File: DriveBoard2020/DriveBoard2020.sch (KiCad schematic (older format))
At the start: 69 parts, among them SW0 SW_SPST, SW1 SW_Push, SW3 SW_Push, SW5 SW_Push, SW7 SW_Push, SW8 SW_Push, SW9 SW_Push, U1 MAX_3232, U2 MAX_3232, U3 OKI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

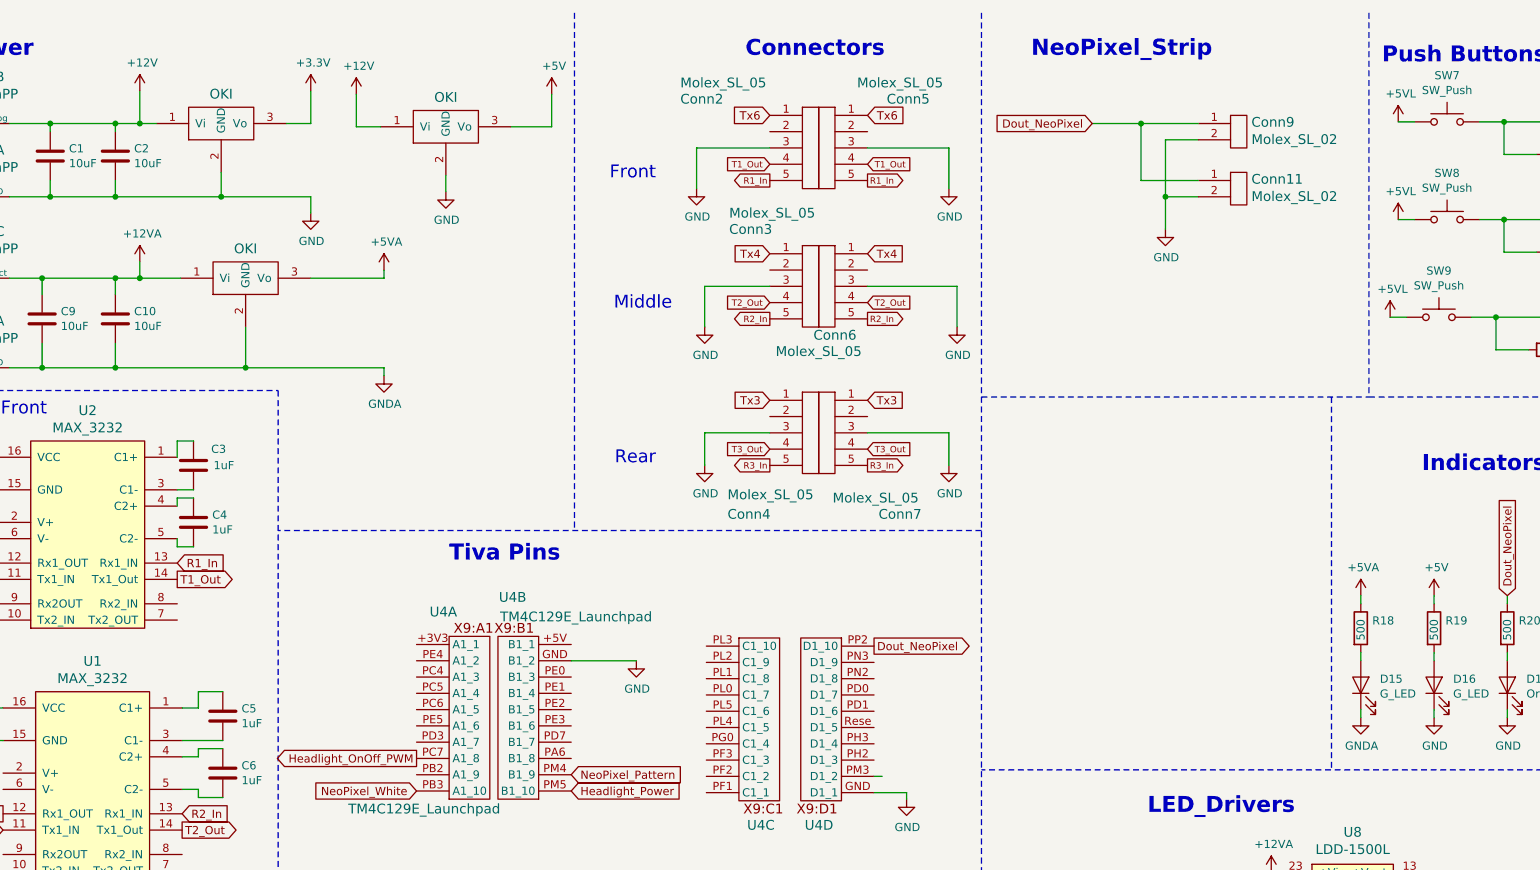
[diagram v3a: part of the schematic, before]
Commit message: cleaned up layout and generated gerbs
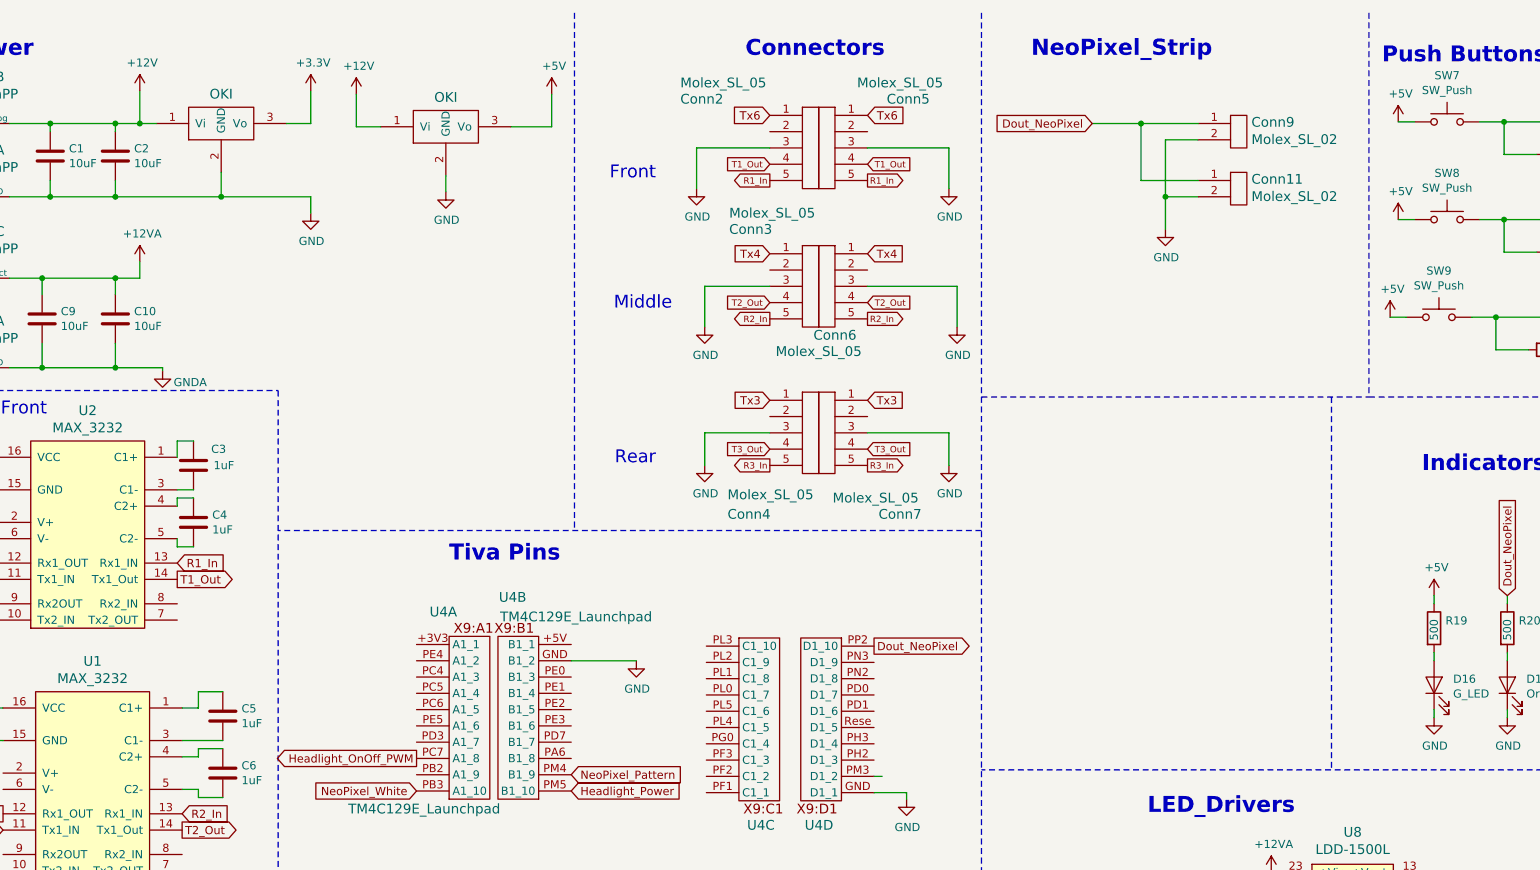
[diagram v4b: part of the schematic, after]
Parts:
- removed D15: G_LED, LED_SMD:LED_0603_1608Metric_Pad1.05x0.95mm_HandSolder, symbol Device:LED
- removed R18: 500, Resistor_SMD:R_0603_1608Metric_Pad1.05x0.95mm_HandSolder, symbol Device:R
- removed U7: OKI, MRDT_Devices:OKI_Horizontal, symbol DriveBoard2020-rescue:OKI-MRDT_Devices-DriveBoard2020-rescue
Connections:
- net +5VL is gone; now on net +5V: SW7.1, SW8.1, SW9.1
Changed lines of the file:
@@
 Indicators
-$Comp
-L Device:R R18
-U 1 1 5C07EDC4
-P 14120 4250
-F 0 "R18" H 14190 4296 50  0000 L CNN
-F 1 "500" V 14120 4175 50  0000 L CNN
-F 2 "Resistor_SMD:R_0603_1608Metric_Pad1.05x0.95mm_HandSolder" V 14050 4250 50  0001 C CNN
-F 3 "~" H 14120 4250 50  0001 C CNN
-	1    14120 4250
-	1    0    0    -1
-$EndComp
 $Comp
 L Device:R R20
@@
 	1    15545 4800
 	1    0    0    -1
-$EndComp
-$Comp
-L Device:LED D15
-U 1 1 5C07F18A
-P 14120 4600
-F 0 "D15" V 14158 4483 50  0000 R CNN
-F 1 "G_LED" V 14067 4483 50  0000 R CNN
-F 2 "LED_SMD:LED_0603_1608Metric_Pad1.05x0.95mm_HandSolder" H 14120 4600 50  0001 C CNN
-F 3 "~" H 14120 4600 50  0001 C CNN
-	1    14120 4600
-	0    -1   -1   0
 $EndComp
 $Comp
@@
 $EndComp
 Wire Wire Line
-	14120 4400 14120 4450
-Wire Wire Line
 	15020 4400 15020 4450
 Wire Wire Line
@@
 Wire Wire Line
 	15545 4750 15545 4800
-Wire Wire Line
-	14120 4100 14120 4050
 Text GLabel 15020 4050 1    50   Input ~ 0
 Dout_NeoPixel
@@
 Wire Wire Line
 	15020 4750 15020 4800
-Wire Wire Line
-	14120 4750 14120 4800
 $Comp
 L power:+12VA #PWR0149
@@
 Wire Wire Line
 	14620 6000 15070 6000
-$Comp
-L power:+5VA #PWR0152
-U 1 1 5C7B3BE6
-P 14120 4050
-F 0 "#PWR0152" H 14120 3900 50  0001 C CNN
-F 1 "+5VA" H 14135 4223 50  0000 C CNN
-F 2 "" H 14120 4050 50  0001 C CNN
-F 3 "" H 14120 4050 50  0001 C CNN
-	1    14120 4050
-	1    0    0    -1
-$EndComp
-$Comp
-L power:GNDA #PWR0156
-U 1 1 5C7A2B5E
-P 14120 4800
-F 0 "#PWR0156" H 14120 4550 50  0001 C CNN
-F 1 "GNDA" H 14125 4627 50  0000 C CNN
-F 2 "" H 14120 4800 50  0001 C CNN
-F 3 "" H 14120 4800 50  0001 C CNN
-	1    14120 4800
-	1    0    0    -1
-$EndComp
-$Comp
-L power:+5VL #PWR0157
-U 1 1 5C7A4D57
-P 14350 1140
-F 0 "#PWR0157" H 14350 990 50  0001 C CNN
-F 1 "+5VL" H 14365 1313 50  0000 C CNN
-F 2 "" H 14350 1140 50  0001 C CNN
-F 3 "" H 14350 1140 50  0001 C CNN
-	1    14350 1140
-	1    0    0    -1
-$EndComp
-$Comp
-L power:+5VL #PWR0158
-U 1 1 5C7A690E
-P 14350 1740
-F 0 "#PWR0158" H 14350 1590 50  0001 C CNN
-F 1 "+5VL" H 14365 1913 50  0000 C CNN
-F 2 "" H 14350 1740 50  0001 C CNN
-F 3 "" H 14350 1740 50  0001 C CNN
-	1    14350 1740
-	1    0    0    -1
-$EndComp
-$Comp
-L power:+5VL #PWR0159
-U 1 1 5C7A8412
-P 14300 2340
-F 0 "#PWR0159" H 14300 2190 50  0001 C CNN
-F 1 "+5VL" H 14315 2513 50  0000 C CNN
-F 2 "" H 14300 2340 50  0001 C CNN
-F 3 "" H 14300 2340 50  0001 C CNN
-	1    14300 2340
-	1    0    0    -1
-$EndComp
 $Comp
 L Device:R R15
@@
 $EndComp
 $Comp
-L MRDT_Connectors:AndersonPP Conn8
-U 3 1 5E2EC70E
-P 5420 2200
-F 0 "Conn8" H 5628 2587 60  0000 C CNN
-F 1 "AndersonPP" H 5628 2481 60  0000 C CNN
-F 2 "MRDT_Connectors:Anderson_2_Horizontal_Side_by_Side" H 5270 1650 60  0001 C CNN
-F 3 "" H 5270 1650 60  0001 C CNN
-	3    5420 2200
-	1    0    0    -1
-$EndComp
-Wire Wire Line
-	6620 2100 6620 2000
-Connection ~ 6620 2100
-Wire Wire Line
-	6620 2100 6870 2100
-$Comp
-L power:+12VA #PWR0164
-U 1 1 5E314225
-P 6620 2000
-F 0 "#PWR0164" H 6620 1850 50  0001 C CNN
-F 1 "+12VA" H 6635 2173 50  0000 C CNN
-F 2 "" H 6620 2000 50  0001 C CNN
-F 3 "" H 6620 2000 50  0001 C CNN
-	1    6620 2000
-	1    0    0    -1
-$EndComp
-$Comp
-L DriveBoard2020-rescue:OKI-MRDT_Devices-DriveBoard2020-rescue U7
-U 1 1 5E314A7F
-P 7070 2200
-F 0 "U7" H 7120 2150 60  0001 C CNN
-F 1 "OKI" H 7270 2481 60  0000 C CNN
-F 2 "MRDT_Devices:OKI_Horizontal" H 6870 2100 60  0001 C CNN
-F 3 "" H 6870 2100 60  0001 C CNN
-	1    7070 2200
-	1    0    0    -1
-$EndComp
-Wire Wire Line
-	7670 2100 8120 2100
-Wire Wire Line
-	8120 2100 8120 2050
-$Comp
-L power:+5VA #PWR0165
-U 1 1 5E339600
-P 8120 2050
-F 0 "#PWR0165" H 8120 1900 50  0001 C CNN
-F 1 "+5VA" H 8135 2223 50  0000 C CNN
-F 2 "" H 8120 2050 50  0001 C CNN
-F 3 "" H 8120 2050 50  0001 C CNN
-	1    8120 2050
-	1    0    0    -1
-$EndComp
-$Comp
-L Device:C C9
-U 1 1 5E34ECB7
-P 6020 2350
-F 0 "C9" H 6135 2396 50  0000 L CNN
-F 1 "10uF" H 6135 2305 50  0000 L CNN
-F 2 "Capacitor_SMD:C_0603_1608Metric_Pad1.05x0.95mm_HandSolder" H 6058 2200 50  0001 C CNN
-F 3 "~" H 6020 2350 50  0001 C CNN
-	1    6020 2350
-	1    0    0    -1
-$EndComp
-Wire Wire Line
-	5820 2100 6020 2100
-Wire Wire Line
-	6020 2200 6020 2100
-Connection ~ 6020 2100
-Wire Wire Line
-	6020 2100 6470 2100
-Wire Wire Line
-	6020 2650 6470 2650
-Wire Wire Line
-	6020 2500 6020 2650
-$Comp
-L Device:C C10
-U 1 1 5E3AB402
-P 6470 2350
-F 0 "C10" H 6585 2396 50  0000 L CNN
-F 1 "10uF" H 6585 2305 50  0000 L CNN
-F 2 "Capacitor_SMD:C_0603_1608Metric_Pad1.05x0.95mm_HandSolder" H 6508 2200 50  0001 C CNN
-F 3 "~" H 6470 2350 50  0001 C CNN
-	1    6470 2350
-	1    0    0    -1
-$EndComp
-Wire Wire Line
-	6470 2200 6470 2100
-Connection ~ 6470 2100
-Wire Wire Line
-	6470 2100 6620 2100
-Wire Wire Line
-	6470 2500 6470 2650
-Connection ~ 6470 2650
-Wire Wire Line
-	6470 2650 7270 2650
-Wire Wire Line
-	7270 2400 7270 2650
-Wire Wire Line
-	7270 2650 8120 2650
-Connection ~ 7270 2650
-Wire Wire Line
-	8120 2650 8120 2700
-$Comp
 L MRDT_Connectors:Molex_SL_02 Conn9
 U 1 1 5DE15636
@@
 	1    0    0    -1
 $EndComp
-$Comp
-L power:GNDA #PWR0151
-U 1 1 5E572CB7
-P 8120 2700
-F 0 "#PWR0151" H 8120 2450 50  0001 C CNN
-F 1 "GNDA" H 8125 2527 50  0000 C CNN
-F 2 "" H 8120 2700 50  0001 C CNN
-F 3 "" H 8120 2700 50  0001 C CNN
-	1    8120 2700
-	1    0    0    -1
-$EndComp
-$Comp
-L MRDT_Connectors:AndersonPP Conn8
-U 1 1 5E595C87
-P 5420 2750
-F 0 "Conn8" H 5628 3137 60  0000 C CNN
-F 1 "AndersonPP" H 5628 3031 60  0000 C CNN
-F 2 "MRDT_Connectors:Anderson_2_Horizontal_Side_by_Side" H 5270 2200 60  0001 C CNN
-F 3 "" H 5270 2200 60  0001 C CNN
-	1    5420 2750
-	1    0    0    -1
-$EndComp
-Wire Wire Line
-	6020 2650 5820 2650
-Connection ~ 6020 2650
 Wire Wire Line
 	6470 1600 7120 1600
@@
 Wire Notes Line style solid
 	8530 7800 8530 11220
+Wire Wire Line
+	6020 2650 5820 2650
+$Comp
+L MRDT_Connectors:AndersonPP Conn8
+U 1 1 5E595C87
+P 5420 2750
+F 0 "Conn8" H 5628 3137 60  0000 C CNN
+F 1 "AndersonPP" H 5628 3031 60  0000 C CNN
+F 2 "MRDT_Connectors:Anderson_2_Horizontal_Side_by_Side" H 5270 2200 60  0001 C CNN
+F 3 "" H 5270 2200 60  0001 C CNN
+	1    5420 2750
+	1    0    0    -1
+$EndComp
+$Comp
+L power:GNDA #PWR0151
+U 1 1 5E572CB7
+P 6760 2670
+F 0 "#PWR0151" H 6760 2420 50  0001 C CNN
+F 1 "GNDA" H 6930 2600 50  0000 C CNN
+F 2 "" H 6760 2670 50  0001 C CNN
+F 3 "" H 6760 2670 50  0001 C CNN
+	1    6760 2670
+	1    0    0    -1
+$EndComp
+Wire Wire Line
+	6470 2500 6470 2650
+Wire Wire Line
+	6470 2200 6470 2100
+$Comp
+L Device:C C10
+U 1 1 5E3AB402
+P 6470 2350
+F 0 "C10" H 6585 2396 50  0000 L CNN
+F 1 "10uF" H 6585 2305 50  0000 L CNN
+F 2 "Capacitor_SMD:C_0603_1608Metric_Pad1.05x0.95mm_HandSolder" H 6508 2200 50  0001 C CNN
+F 3 "~" H 6470 2350 50  0001 C CNN
+	1    6470 2350
+	1    0    0    -1
+$EndComp
+Wire Wire Line
+	6020 2500 6020 2650
+Connection ~ 6020 2650
+Wire Wire Line
+	6020 2650 6470 2650
+Connection ~ 6470 2100
+Wire Wire Line
+	6020 2100 6470 2100
+Wire Wire Line
+	6020 2200 6020 2100
+Connection ~ 6020 2100
+Wire Wire Line
+	5820 2100 6020 2100
+$Comp
+L Device:C C9
+U 1 1 5E34ECB7
+P 6020 2350
+F 0 "C9" H 6135 2396 50  0000 L CNN
+F 1 "10uF" H 6135 2305 50  0000 L CNN
+F 2 "Capacitor_SMD:C_0603_1608Metric_Pad1.05x0.95mm_HandSolder" H 6058 2200 50  0001 C CNN
+F 3 "~" H 6020 2350 50  0001 C CNN
+	1    6020 2350
+	1    0    0    -1
+$EndComp
+$Comp
+L power:+12VA #PWR0164
+U 1 1 5E314225
+P 6620 2000
+F 0 "#PWR0164" H 6620 1850 50  0001 C CNN
+F 1 "+12VA" H 6635 2173 50  0000 C CNN
+F 2 "" H 6620 2000 50  0001 C CNN
+F 3 "" H 6620 2000 50  0001 C CNN
+	1    6620 2000
+	1    0    0    -1
+$EndComp
+Wire Wire Line
+	6470 2100 6620 2100
+Wire Wire Line
+	6620 2100 6620 2000
+$Comp
+L MRDT_Connectors:AndersonPP Conn8
+U 3 1 5E2EC70E
+P 5420 2200
+F 0 "Conn8" H 5628 2587 60  0000 C CNN
+F 1 "AndersonPP" H 5628 2481 60  0000 C CNN
+F 2 "MRDT_Connectors:Anderson_2_Horizontal_Side_by_Side" H 5270 1650 60  0001 C CNN
+F 3 "" H 5270 1650 60  0001 C CNN
+	3    5420 2200
+	1    0    0    -1
+$EndComp
+Wire Wire Line
+	6470 2650 6760 2650
+Wire Wire Line
+	6760 2650 6760 2670
+Connection ~ 6470 2650
+$Comp
+L power:+5V #PWR?
+U 1 1 5DEF90AA
+P 14300 2340
+F 0 "#PWR?" H 14300 2190 50  0001 C CNN
+F 1 "+5V" H 14315 2513 50  0000 C CNN
+F 2 "" H 14300 2340 50  0001 C CNN
+F 3 "" H 14300 2340 50  0001 C CNN
+	1    14300 2340
+	1    0    0    -1
+$EndComp
+$Comp
+L power:+5V #PWR?
+U 1 1 5DEFA30D
+P 14350 1740
+F 0 "#PWR?" H 14350 1590 50  0001 C CNN
+F 1 "+5V" H 14365 1913 50  0000 C CNN
+F 2 "" H 14350 1740 50  0001 C CNN
+F 3 "" H 14350 1740 50  0001 C CNN
+	1    14350 1740
+	1    0    0    -1
+$EndComp
+$Comp
+L power:+5V #PWR?
+U 1 1 5DEFAF75
+P 14350 1140
+F 0 "#PWR?" H 14350 990 50  0001 C CNN
+F 1 "+5V" H 14365 1313 50  0000 C CNN
+F 2 "" H 14350 1140 50  0001 C CNN
+F 3 "" H 14350 1140 50  0001 C CNN
+	1    14350 1140
+	1    0    0    -1
+$EndComp
 $EndSCHEMATC

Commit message: Worked on grids
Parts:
- removed C3, C4, C5, C6, C7, C8: 1uF, Capacitor_SMD:C_0603_1608Metric_Pad1.05x0.95mm_HandSolder, symbol Device:C
- added C? (x6): 1uF, symbol Device:C_Small
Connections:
- net GNDA is gone; now on net GND: C10.2, C9.2, Conn8.1 (GND)
- net +3V3: now also SW7.1
- net +5V: no longer SW7.1, SW8.1
- net Tx3: no longer Conn4.1, Conn7.1
- net Tx4: no longer Conn3.1, Conn6.1
- net Tx6: no longer Conn2.1, Conn5.1
- net at U1.1 (C1+): now also C?.1
- net at U1.3 (C1-): now also C?.2
- net at U1.4 (C2+): now also C?.1
- net at U1.5 (C2-): now also C?.2
- net at U2.3 (C1-): now also C?.2
- net at U2.1 (C1+): now also C?.1
- net at U2.4 (C2+): now also C?.1
- net at U2.5 (C2-): now also C?.2
- net at U5.1 (C1+): now also C?.1
- net at U5.3 (C1-): now also C?.2
- net at U5.4 (C2+): now also C?.1
- net at U5.5 (C2-): now also C?.2
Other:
- moved on the sheet: C1, C10, C2, C9, Conn1A, Conn1B, Conn8A, Conn8C, R15, R16, SW7, SW8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
